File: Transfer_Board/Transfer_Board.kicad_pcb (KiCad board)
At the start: 2 copper layers, 51 x 53 mm, 14 parts

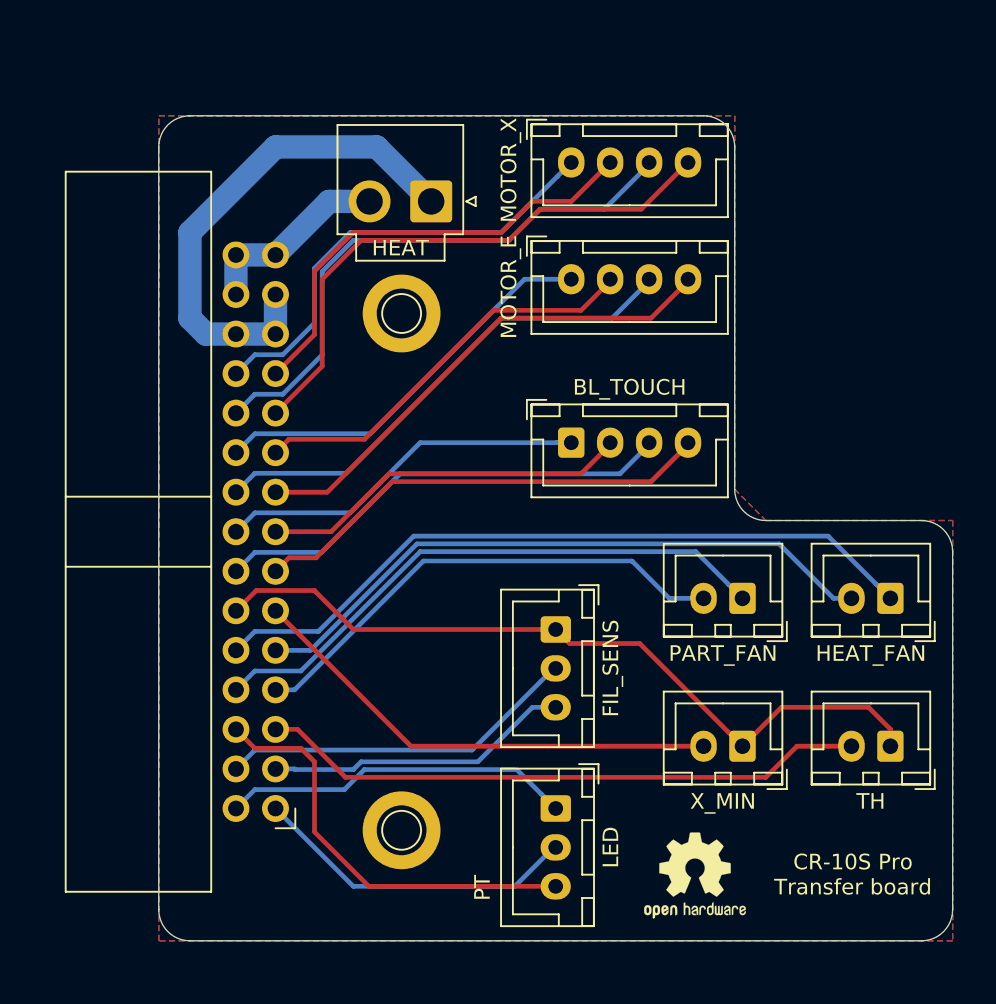
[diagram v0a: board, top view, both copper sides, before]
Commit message: Modified to allow use of Duet3D control boards
Modified the Transfer Board to allow use of Duet3D control boards.  The following changes have been made: relocated connectors, removed LED connector to free-up pins for fully independent signal routing (eliminated shared grounds and power), added shared Z_MIN connector for stock capacitive probe, widened and doubled MOTOR and HEAT traces for improved current capacity, widened all other traces, relocated TH signal wires to the edge of the ribbon cable, away from “noisy” signals.
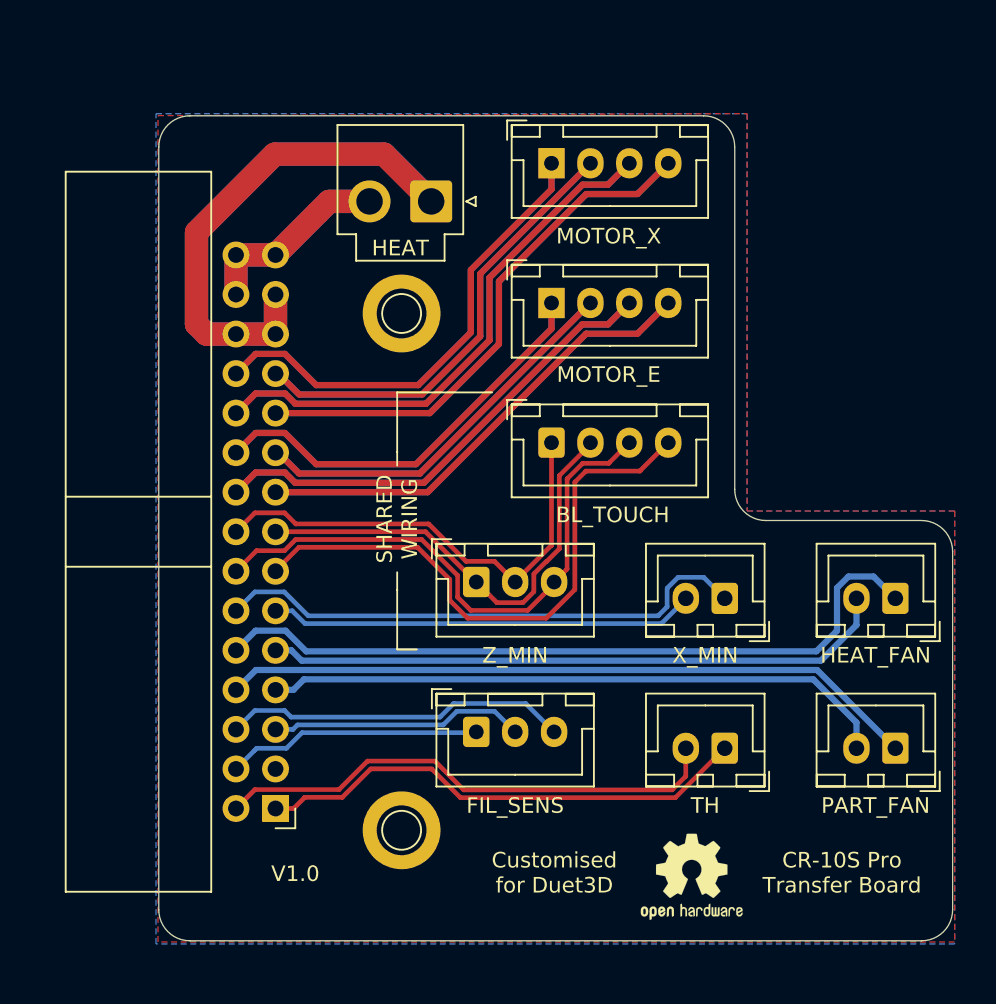
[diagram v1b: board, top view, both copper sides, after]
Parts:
- moved Z_MIN 15.4 mm to (120.4, 77.0), turned to 0 degrees
- moved PART_FAN 13.8 mm to (147.3, 87.6)
- moved TH 10.6 mm to (136.4, 87.6)
- moved X_MIN 9.57 mm to (136.4, 78.0)
- moved FIL_SENS 8.33 mm to (120.4, 86.6), turned to 0 degrees
- moved MOTOR_E 1.98 mm to (125.2, 59.0)
- moved MOTOR_X 1.27 mm to (125.2, 50.0)
- moved BL_TOUCH 1.27 mm to (125.2, 68.0)
- moved HEAT_FAN 0.32 mm to (147.3, 78.0)
- moved REF** 0.23 mm to (134.2, 95.9)
- renumbered LED to Z_MIN
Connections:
- RIBBON1 pad 1: Net-(LED1-Pad2) -> Net-(RIBBON1-Pad1)
- RIBBON1 pad 12: Net-(FIL_SENS1-Pad1) -> Net-(RIBBON1-Pad12)
- RIBBON1 pad 2: Net-(LED1-Pad1) -> Net-(RIBBON1-Pad2)
- RIBBON1 pad 3: Net-(FIL_SENS1-Pad3) -> Net-(RIBBON1-Pad3)
- RIBBON1 pad 4: Net-(FIL_SENS1-Pad2) -> Net-(FIL_SENS1-Pad1)
- RIBBON1 pad 5: Net-(RIBBON1-Pad5) -> Net-(FIL_SENS1-Pad2)
- RIBBON1 pad 6: Net-(LED1-Pad3) -> Net-(FIL_SENS1-Pad3)
- TH pad 1: Net-(FIL_SENS1-Pad1) -> Net-(RIBBON1-Pad1)
- TH pad 2: Net-(RIBBON1-Pad5) -> Net-(RIBBON1-Pad2)
- X_MIN pad 1: Net-(FIL_SENS1-Pad1) -> Net-(RIBBON1-Pad12)
- Z_MIN pad 1: Net-(LED1-Pad1) -> Net-(BL_TOUCH1-Pad2)
- Z_MIN pad 2: Net-(LED1-Pad2) -> Net-(BL_TOUCH1-Pad1)
- Z_MIN pad 3: Net-(LED1-Pad3) -> Net-(BL_TOUCH1-Pad3)
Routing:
- net Net-(RIBBON1-Pad5): track 39.1 -> 0.00 mm
- net Net-(RIBBON1-Pad12): track 0.00 -> 34.8 mm
- net Net-(MOTOR_X1-Pad3): track 36.4 -> 69.6 mm
- net Net-(RIBBON1-Pad2): track 0.00 -> 33.1 mm
- net Net-(FIL_SENS1-Pad1): track 49.4 -> 16.4 mm
- net Net-(RIBBON1-Pad1): track 0.00 -> 32.8 mm
- net Net-(MOTOR_X1-Pad1): track 29.2 -> 61.7 mm
- net Net-(MOTOR_X1-Pad4): track 36.4 -> 68.5 mm
- net Net-(HEAT1-Pad1): track 33.2 -> 64.4 mm
- net Net-(MOTOR_E1-Pad3): track 32.3 -> 61.7 mm
- net Net-(MOTOR_X1-Pad2): track 29.5 -> 58.6 mm
- net Net-(MOTOR_E1-Pad4): track 32.2 -> 60.5 mm
- net Net-(MOTOR_E1-Pad1): track 26.2 -> 53.8 mm
- net Net-(LED1-Pad3): track 27.4 -> 0.00 mm
- net Net-(MOTOR_E1-Pad2): track 26.2 -> 50.7 mm
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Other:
- board text added: "+24V"
- board text added: "+5V SIG"
- board text added: "A- A+"
- board text added: "B- B+"
- board text added: "CR-10S Pro Transfer Board"
- board text added: "CTRL PWR"
- board text added: "Customised for Duet3D"
- board text added: "FS"
- board text added: "GND"
- board text added: "H"
- board text added: "HF"
- board text added: "ME"
- board text added: "MX"
- board text added: "N/C GND"
- board text added: "PF"
- board text added: "PWR GND"
- board text added: "SHARED WIRING"
- board text added: "SIG"
- board text added: "SIG GND"
- board text added: "TH"
- board text added: "V1.0"
- board text added: "WARNING: BL_TOUCH AND Z_MIN SHARE WIRING, CONNECT PWR TO +5V FOR BL_TOUCH OR +24V FOR Z_MIN (STOCK) PROBE."
- board text added: "X-"
- board text added: "Z-"
- board text removed: "CR-10S Pro Transfer board"
- board text removed: "PT"

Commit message: Revised board to v1.1
Corrected original board geometry errors and incorporated additional improvements.
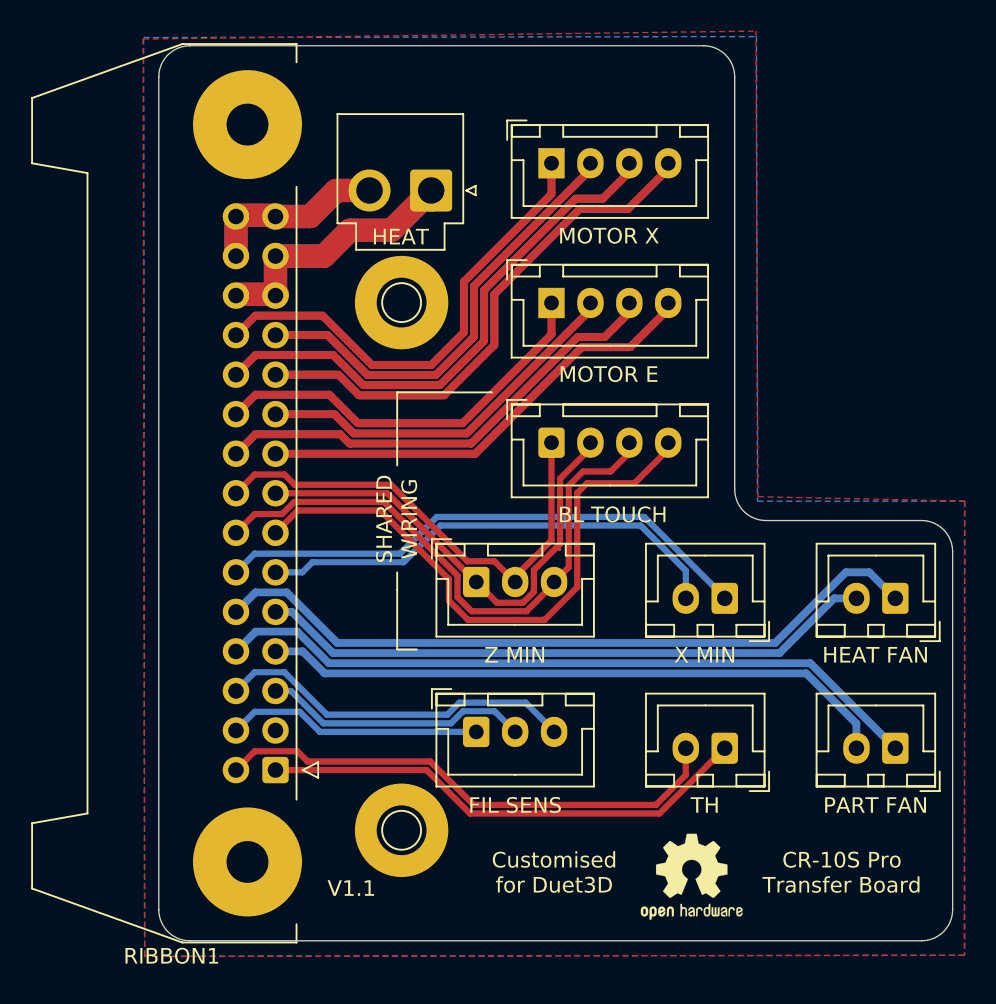
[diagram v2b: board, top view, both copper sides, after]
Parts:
- BL TOUCH: renamed from BL_TOUCH
- FIL SENS: renamed from FIL_SENS
- HEAT FAN: renamed from HEAT_FAN
- MOTOR E: renamed from MOTOR_E
- MOTOR X: renamed from MOTOR_X
- PART FAN: renamed from PART_FAN
- RIBBON1: footprint Connector_IDC:IDC-Header_2x15_P2.54mm_Horizontal -> Connector_IDC:IDC-Header_2x15-1MP_P2.54mm_Latch_Horizontal
- X MIN: renamed from X_MIN
- Z MIN: renamed from Z_MIN
- moved RIBBON1 2.47 mm to (107.5, 89.0)
- moved HEAT 0.70 mm to (117.5, 51.8)
- moved REF** 0.70 mm to (115.6, 59.0)
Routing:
- net Net-(HEAT1-Pad1): track 64.4 -> 34.4 mm
- net Net-(RIBBON1-Pad11): track 27.8 -> 31.5 mm
- net Net-(MOTOR_E1-Pad1): track 53.8 -> 51.7 mm
- net Net-(MOTOR_E1-Pad2): track 50.7 -> 49.1 mm
- net Net-(HEAT1-Pad2): track 25.1 -> 23.6 mm
- net Net-(MOTOR_E1-Pad3): track 61.7 -> 60.3 mm
- net Net-(BL_TOUCH1-Pad3): track 37.4 -> 38.9 mm
- net Net-(MOTOR_E1-Pad4): track 60.5 -> 59.4 mm
- net Net-(BL_TOUCH1-Pad2): track 29.9 -> 31.0 mm
- net Net-(BL_TOUCH1-Pad1): track 30.2 -> 31.2 mm
- net Net-(PART_FAN1-Pad1): track 45.0 -> 46.0 mm
- net Net-(FIL_SENS1-Pad3): track 22.2 -> 23.2 mm
- net Net-(FIL_SENS1-Pad2): track 16.8 -> 17.5 mm
- net Net-(HEAT_FAN1-Pad1): track 47.6 -> 46.8 mm
- net Net-(MOTOR_X1-Pad1): track 61.7 -> 61.0 mm
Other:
- board size 51 x 53 mm -> 51 x 57.5 mm
- net class Default: clearance 0.2 -> 0.1524; trace_width 0.25 -> 0.1524; via_dia 0.8 -> 0.6858; via_drill 0.4 -> 0.3302
- rule pad_to_mask_clearance: 0.051 -> 0.0508
- rule solder_mask_min_width: 0.25 -> 0.1016
- rule trace_clearance: 0.2 -> 0.1524
- rule trace_min: 0.2 -> 0.1524
- rule via_min_drill: 0.3 -> 0.254
- rule via_min_size: 0.4 -> 0.508
- board text added: "A-+"
- board text added: "B-+"
- board text added: "V1.1"
- board text added: "VSSA SIG"
- board text added: "WARNING: BL TOUCH AND Z MIN SHARE WIRING, CONNECT PWR TO +5V FOR BL TOUCH OR +24V FOR Z MIN (STOCK) PROBE."
- board text removed: "A- A+"
- board text removed: "B- B+"
- board text removed: "SIG"
- board text removed: "V1.0"
- board text removed: "WARNING: BL_TOUCH AND Z_MIN SHARE WIRING, CONNECT PWR TO +5V FOR BL_TOUCH OR +24V FOR Z_MIN (STOCK) PROBE."

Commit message: Bottom silkscreen correction
Corrected TH pin assignment on bottom silkscreen.  Small tweaks to README.md.
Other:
- board text added: "SIG VSSA"
- board text removed: "VSSA SIG"

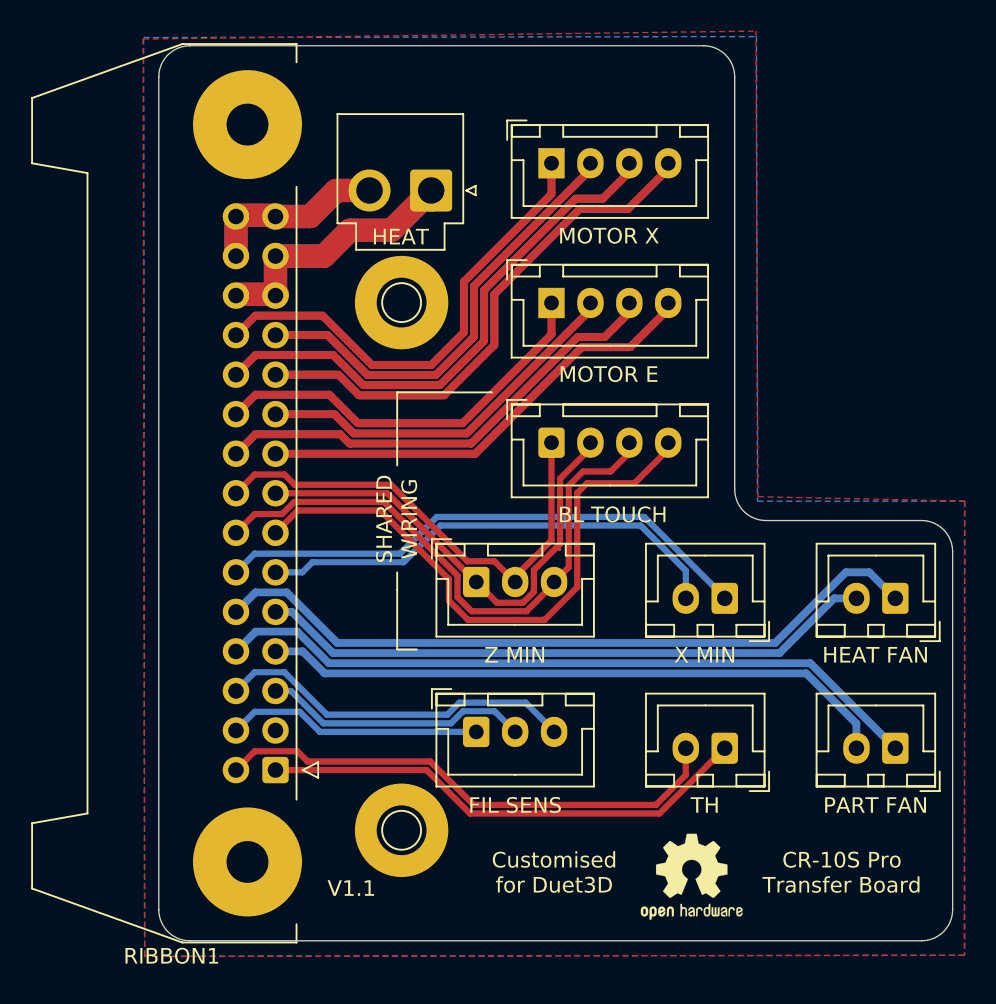
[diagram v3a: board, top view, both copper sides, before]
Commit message: Rationalization of connector pinouts and ribbon cable assignments
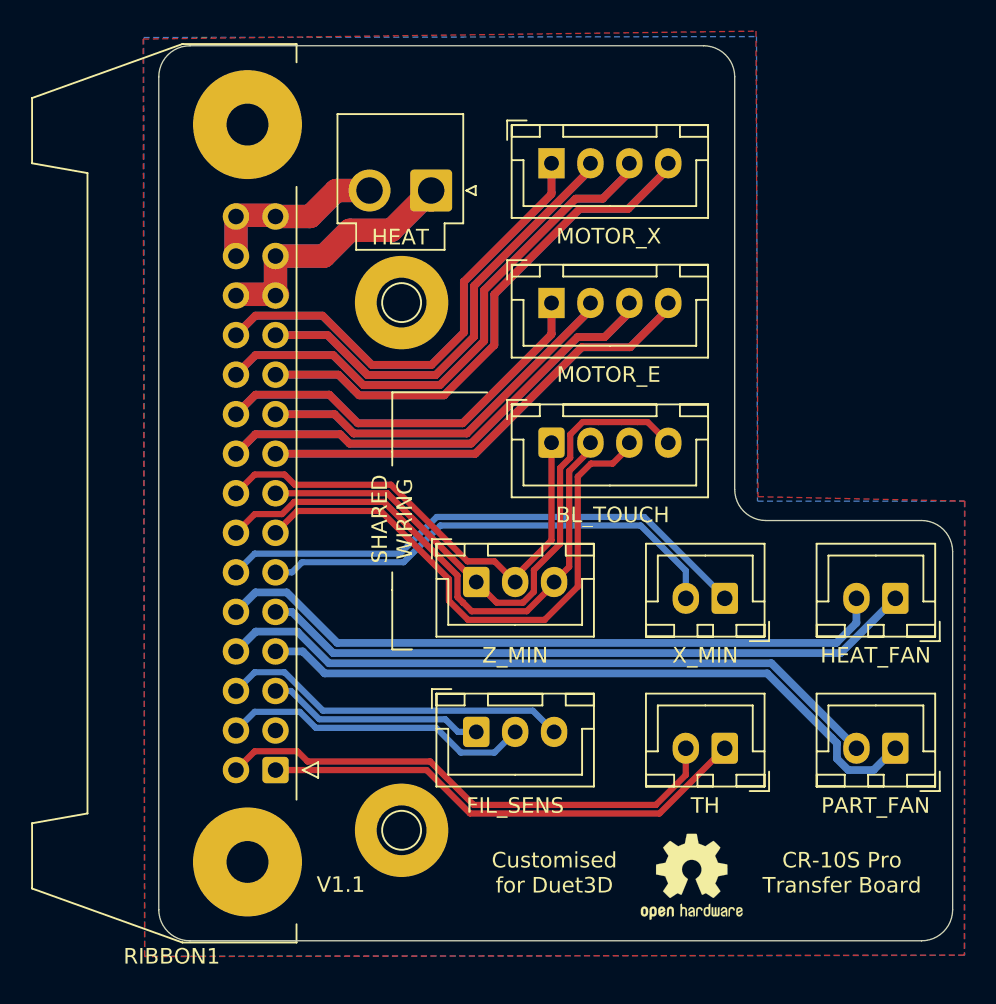
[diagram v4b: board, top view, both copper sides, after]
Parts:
- BL_TOUCH: renamed from BL TOUCH
- FIL_SENS: renamed from FIL SENS
- HEAT_FAN: renamed from HEAT FAN
- MOTOR_E: renamed from MOTOR E
- MOTOR_X: renamed from MOTOR X
- PART_FAN: renamed from PART FAN
- X_MIN: renamed from X MIN
- Z_MIN: renamed from Z MIN
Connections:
- net Net-(BL_TOUCH1-Pad1) renamed /GND
- BL_TOUCH pad 2: Net-(BL_TOUCH1-Pad2) -> /+5V
- BL_TOUCH pad 3: Net-(BL_TOUCH1-Pad3) -> /CTRL
- BL_TOUCH pad 4: Net-(BL_TOUCH1-Pad4) -> /SIG
- RIBBON1 pad 10: Net-(HEAT_FAN1-Pad1) -> Net-(HEAT_FAN1-Pad2)
- RIBBON1 pad 13: Net-(BL_TOUCH1-Pad4) -> /CTRL
- RIBBON1 pad 14: Net-(BL_TOUCH1-Pad3) -> /+5V
- RIBBON1 pad 15: Net-(BL_TOUCH1-Pad2) -> /SIG
- RIBBON1 pad 4: Net-(FIL_SENS1-Pad1) -> Net-(FIL_SENS1-Pad2)
- RIBBON1 pad 5: Net-(FIL_SENS1-Pad2) -> Net-(FIL_SENS1-Pad1)
- RIBBON1 pad 7: Net-(PART_FAN1-Pad2) -> Net-(PART_FAN1-Pad1)
- RIBBON1 pad 8: Net-(PART_FAN1-Pad1) -> Net-(PART_FAN1-Pad2)
- RIBBON1 pad 9: Net-(HEAT_FAN1-Pad2) -> Net-(HEAT_FAN1-Pad1)
- Z_MIN pad 1: Net-(BL_TOUCH1-Pad2) -> /SIG
- Z_MIN pad 3: Net-(BL_TOUCH1-Pad3) -> /+5V
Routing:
- net Net-(BL_TOUCH1-Pad3): track 38.9 -> 0.00 mm
- net Net-(BL_TOUCH1-Pad4): track 38.1 -> 0.00 mm
- net /SIG: track 0.00 -> 38.0 mm
- net /CTRL: track 0.00 -> 36.8 mm
- net /+5V: track 0.00 -> 35.7 mm
- net Net-(BL_TOUCH1-Pad2): track 31.0 -> 0.00 mm
- net Net-(HEAT_FAN1-Pad1): track 46.8 -> 42.7 mm
- net Net-(HEAT_FAN1-Pad2): track 40.3 -> 43.9 mm
- net Net-(FIL_SENS1-Pad2): track 17.5 -> 20.9 mm
- net Net-(PART_FAN1-Pad2): track 40.8 -> 43.5 mm
- net Net-(FIL_SENS1-Pad1): track 16.6 -> 14.1 mm
- net Net-(PART_FAN1-Pad1): track 46.0 -> 44.1 mm
- net Net-(FIL_SENS1-Pad3): track 23.2 -> 22.6 mm
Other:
- board text added: "SIG +5V"
- board text added: "WARNING: BL_TOUCH AND Z_MIN SHARE WIRING, CONNECT PWR TO +5V FOR BL_TOUCH OR +24V FOR Z_MIN (STOCK) PROBE."
- board text removed: "+5V SIG"
- board text removed: "WARNING: BL TOUCH AND Z MIN SHARE WIRING, CONNECT PWR TO +5V FOR BL TOUCH OR +24V FOR Z MIN (STOCK) PROBE."
